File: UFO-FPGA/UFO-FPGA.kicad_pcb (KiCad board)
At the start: 2 copper layers, 68.6 x 53.3 mm, 84 parts, among them J1 Power, J2 Digital, J3 Digital/PWM, J4 Digital, J5 USB_B_Micro, Q1 2N7002, SW2 SW_DIP_x01, U1 ICE40HX8K-BG121, U10 TL071, U11 TL071, U2 FT2232HL, U3 ASDMB-12MHz, U4 MC34063AD, U5 93LC56CT-I/MS, U6 PWR convert, U7 PWR convert, U8 ADC, U9 N25Q032A13ESC40F

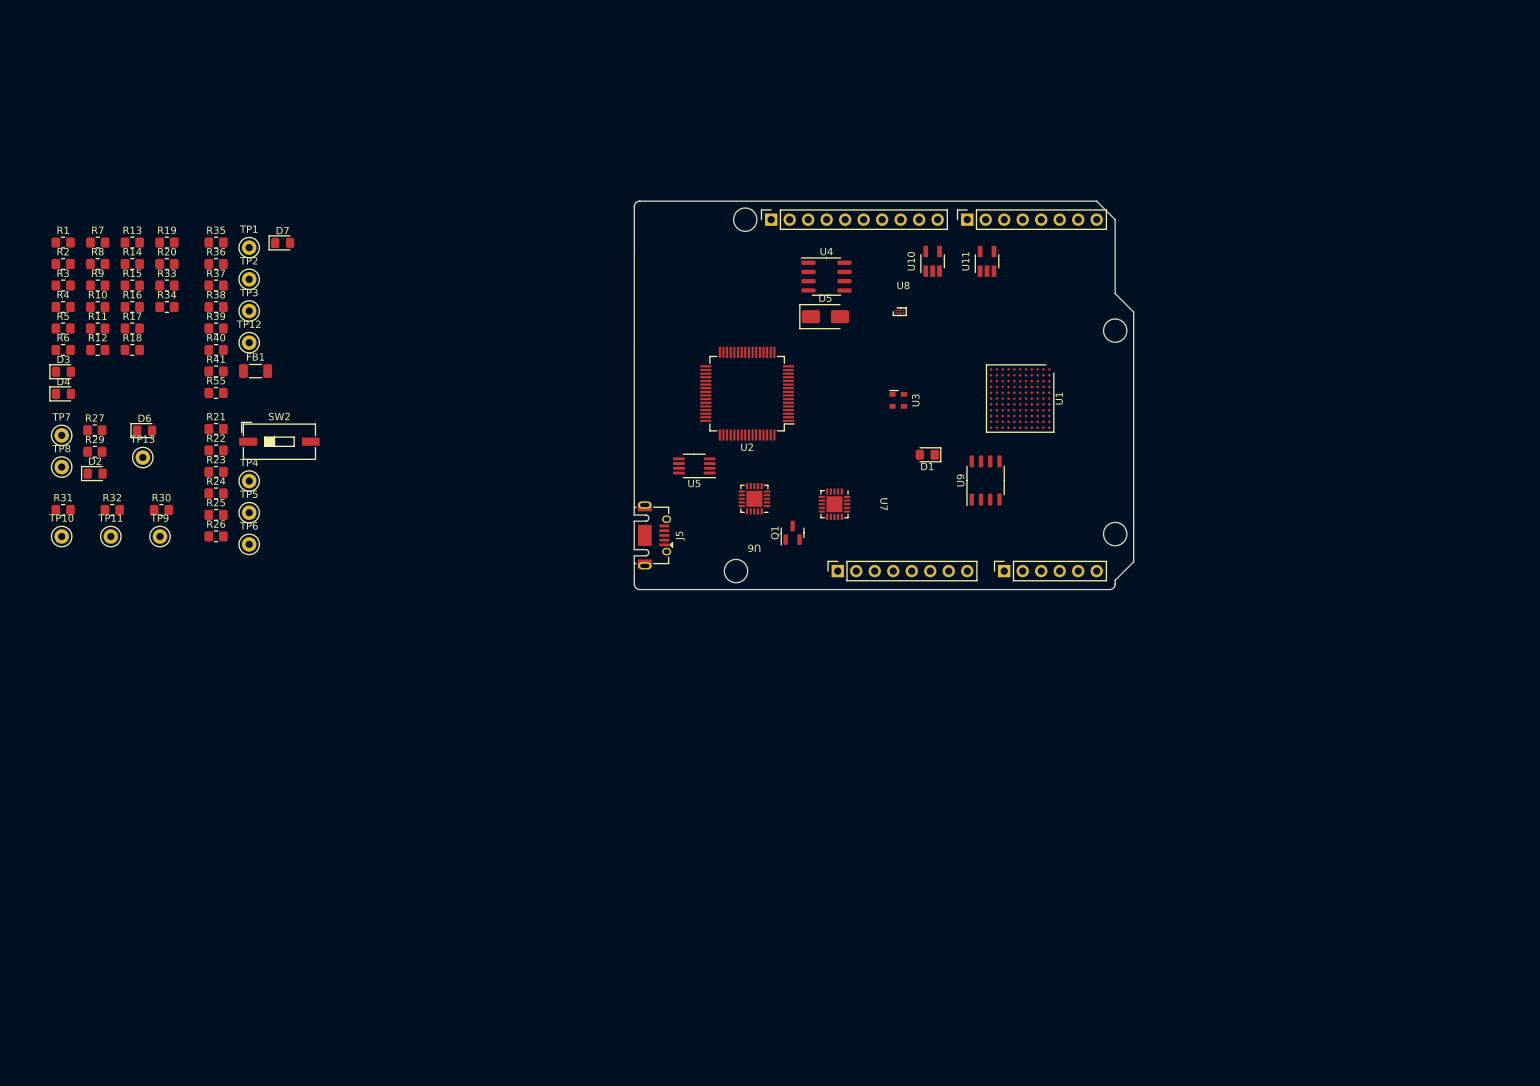
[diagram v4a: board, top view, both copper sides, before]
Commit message: PCB planes
Added:
added Power plane +1v2, +3v3 and +5v on layer 4
Ground plane on layer 2 and 5
Added signal layer 1,3 and 6
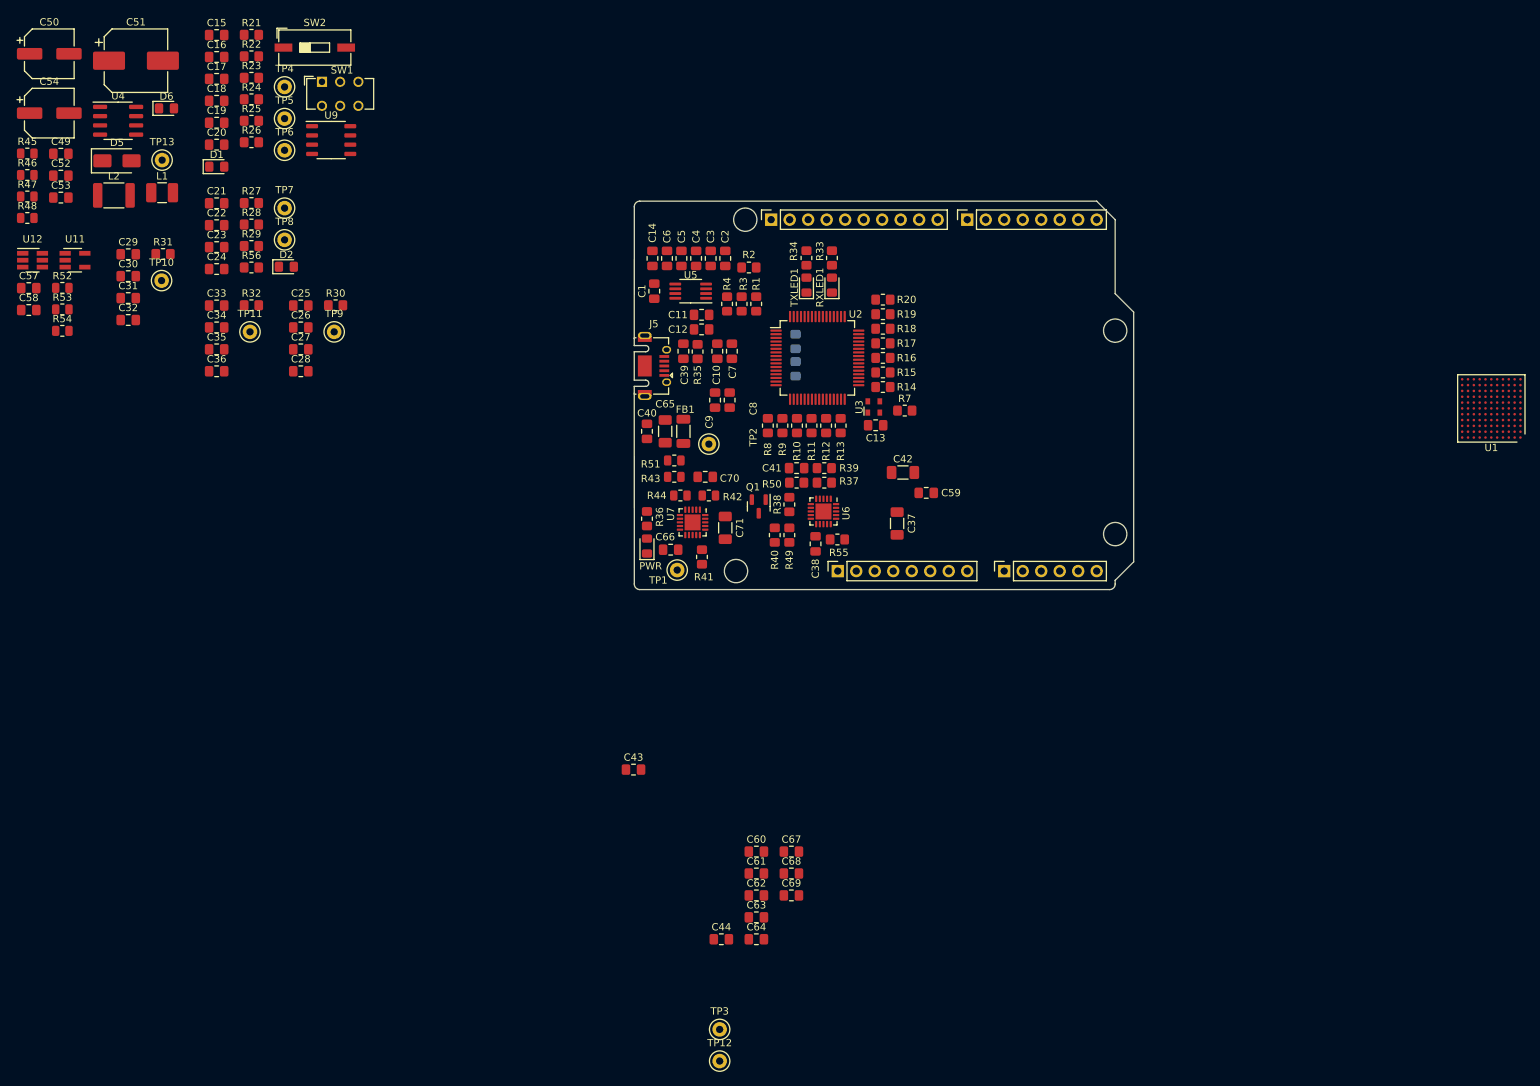
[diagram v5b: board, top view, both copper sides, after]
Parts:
- removed D3: RXLED, LED_SMD:LED_0805_2012Metric_Pad1.15x1.40mm_HandSolder
- removed D4: TXLED, LED_SMD:LED_0805_2012Metric_Pad1.15x1.40mm_HandSolder
- removed D7: POWER, LED_SMD:LED_0805_2012Metric_Pad1.15x1.40mm_HandSolder
- removed U10: TL071, Package_TO_SOT_SMD:SOT-23-5_HandSoldering
- removed U8: ADC, UFO-Footpints:WLP-8
- added C1: 100nF, Capacitor_SMD:C_0805_2012Metric_Pad1.18x1.45mm_HandSolder, F.Cu at (114.2, 60.5)
- added C10: 4u7F, Capacitor_SMD:C_0805_2012Metric_Pad1.18x1.45mm_HandSolder, F.Cu at (122.9, 68.8)
- added C11: 10uF, Capacitor_SMD:C_0805_2012Metric_Pad1.18x1.45mm_HandSolder, F.Cu at (120.8, 63.8)
- added C12: 100nF, Capacitor_SMD:C_0805_2012Metric_Pad1.18x1.45mm_HandSolder, F.Cu at (120.8, 65.8)
- added C13: 100nF, Capacitor_SMD:C_0805_2012Metric_Pad1.18x1.45mm_HandSolder, F.Cu at (144.7, 78.9)
- added C14: 100nF, Capacitor_SMD:C_0805_2012Metric_Pad1.18x1.45mm_HandSolder, F.Cu at (114.0, 56.0)
- added C15: 100nF, Capacitor_SMD:C_0805_2012Metric_Pad1.18x1.45mm_HandSolder, F.Cu at (54.2, 25.3)
- added C16: 100nF, Capacitor_SMD:C_0805_2012Metric_Pad1.18x1.45mm_HandSolder, F.Cu at (54.2, 28.3)
- added C17: 100nF, Capacitor_SMD:C_0805_2012Metric_Pad1.18x1.45mm_HandSolder, F.Cu at (54.2, 31.4)
- added C18: 10uF, Capacitor_SMD:C_0805_2012Metric_Pad1.18x1.45mm_HandSolder, F.Cu at (54.2, 34.4)
- added C19: 10uF, Capacitor_SMD:C_0805_2012Metric_Pad1.18x1.45mm_HandSolder, F.Cu at (54.2, 37.4)
- added C2: 100nF, Capacitor_SMD:C_0805_2012Metric_Pad1.18x1.45mm_HandSolder, F.Cu at (124.0, 56.0)
- added C20: 100nF, Capacitor_SMD:C_0805_2012Metric_Pad1.18x1.45mm_HandSolder, F.Cu at (54.2, 40.4)
- added C21: 100nF, Capacitor_SMD:C_0805_2012Metric_Pad1.18x1.45mm_HandSolder, F.Cu at (54.2, 48.4)
- added C22: 100nF, Capacitor_SMD:C_0805_2012Metric_Pad1.18x1.45mm_HandSolder, F.Cu at (54.2, 51.4)
- added C23: 100nF, Capacitor_SMD:C_0805_2012Metric_Pad1.18x1.45mm_HandSolder, F.Cu at (54.2, 54.5)
- added C24: 100nF, Capacitor_SMD:C_0805_2012Metric_Pad1.18x1.45mm_HandSolder, F.Cu at (54.2, 57.5)
- added C25: 100nF, Capacitor_SMD:C_0805_2012Metric_Pad1.18x1.45mm_HandSolder, F.Cu at (65.7, 62.5)
- added C26: 100nF, Capacitor_SMD:C_0805_2012Metric_Pad1.18x1.45mm_HandSolder, F.Cu at (65.7, 65.5)
- added C27: 100nF, Capacitor_SMD:C_0805_2012Metric_Pad1.18x1.45mm_HandSolder, F.Cu at (65.7, 68.5)
- added C28: 100nF, Capacitor_SMD:C_0805_2012Metric_Pad1.18x1.45mm_HandSolder, F.Cu at (65.7, 71.5)
- added C29: 100nF, Capacitor_SMD:C_0805_2012Metric_Pad1.18x1.45mm_HandSolder, F.Cu at (42.0, 55.4)
- added C3: 100nF, Capacitor_SMD:C_0805_2012Metric_Pad1.18x1.45mm_HandSolder, F.Cu at (122.0, 56.0)
- added C30: 100nF, Capacitor_SMD:C_0805_2012Metric_Pad1.18x1.45mm_HandSolder, F.Cu at (42.0, 58.4)
- added C31: 100nF, Capacitor_SMD:C_0805_2012Metric_Pad1.18x1.45mm_HandSolder, F.Cu at (42.0, 61.5)
- added C32: 100nF, Capacitor_SMD:C_0805_2012Metric_Pad1.18x1.45mm_HandSolder, F.Cu at (42.0, 64.5)
- added C33: 100nF, Capacitor_SMD:C_0805_2012Metric_Pad1.18x1.45mm_HandSolder, F.Cu at (54.2, 62.5)
- added C34: 100nF, Capacitor_SMD:C_0805_2012Metric_Pad1.18x1.45mm_HandSolder, F.Cu at (54.2, 65.5)
- added C35: 100nF, Capacitor_SMD:C_0805_2012Metric_Pad1.18x1.45mm_HandSolder, F.Cu at (54.2, 68.5)
- added C36: 100nF, Capacitor_SMD:C_0805_2012Metric_Pad1.18x1.45mm_HandSolder, F.Cu at (54.2, 71.5)
- added C37: 47uF, Capacitor_SMD:C_1206_3216Metric_Pad1.33x1.80mm_HandSolder, F.Cu at (147.6, 92.4)
- added C38: 10nF, Capacitor_SMD:C_0805_2012Metric_Pad1.18x1.45mm_HandSolder, F.Cu at (136.4, 95.2)
- added C39: 100nF, Capacitor_SMD:C_0805_2012Metric_Pad1.18x1.45mm_HandSolder, F.Cu at (118.2, 68.8)
- added C4: 100nF, Capacitor_SMD:C_0805_2012Metric_Pad1.18x1.45mm_HandSolder, F.Cu at (120.0, 56.0)
- added C40: 100nF, Capacitor_SMD:C_0805_2012Metric_Pad1.18x1.45mm_HandSolder, F.Cu at (113.2, 79.8)
- added C41: 10nF, Capacitor_SMD:C_0805_2012Metric_Pad1.18x1.45mm_HandSolder, F.Cu at (133.8, 84.8)
- added C42: 47uF, Capacitor_SMD:C_1206_3216Metric_Pad1.33x1.80mm_HandSolder, F.Cu at (148.4, 85.4)
- added C43: 10uF, Capacitor_SMD:C_0805_2012Metric_Pad1.18x1.45mm_HandSolder, F.Cu at (111.4, 126.2)
- added C44: 10uF, Capacitor_SMD:C_0805_2012Metric_Pad1.18x1.45mm_HandSolder, F.Cu at (123.5, 149.5)
- added C49: 220pF, Capacitor_SMD:C_0805_2012Metric_Pad1.18x1.45mm_HandSolder, F.Cu at (32.8, 41.6)
- added C5: 100nF, Capacitor_SMD:C_0805_2012Metric_Pad1.18x1.45mm_HandSolder, F.Cu at (118.0, 56.0)
- added C50: 100uF, Capacitor_SMD:CP_Elec_6.3x7.7, F.Cu at (31.2, 27.9)
- added C51: 470uF, Capacitor_SMD:CP_Elec_8x10.5, F.Cu at (43.1, 28.9)
- added C52: 100nF, Capacitor_SMD:C_0805_2012Metric_Pad1.18x1.45mm_HandSolder, F.Cu at (32.8, 44.6)
- added C53: 100nF, Capacitor_SMD:C_0805_2012Metric_Pad1.18x1.45mm_HandSolder, F.Cu at (32.8, 47.6)
- added C54: 100uF, Capacitor_SMD:CP_Elec_6.3x7.7, F.Cu at (31.2, 36.0)
- added C57: 100pF, Capacitor_SMD:C_0805_2012Metric_Pad1.18x1.45mm_HandSolder, F.Cu at (28.4, 60.1)
- added C58: 100pF, Capacitor_SMD:C_0805_2012Metric_Pad1.18x1.45mm_HandSolder, F.Cu at (28.4, 63.1)
- added C59: 1uF, Capacitor_SMD:C_0805_2012Metric_Pad1.18x1.45mm_HandSolder, F.Cu at (151.6, 88.2)
- added C6: 100nF, Capacitor_SMD:C_0805_2012Metric_Pad1.18x1.45mm_HandSolder, F.Cu at (116.0, 56.0)
- added C60: 1uF, Capacitor_SMD:C_0805_2012Metric_Pad1.18x1.45mm_HandSolder, F.Cu at (128.3, 137.5)
- added C61: 100nF, Capacitor_SMD:C_0805_2012Metric_Pad1.18x1.45mm_HandSolder, F.Cu at (128.3, 140.5)
- added C62: 100nF, Capacitor_SMD:C_0805_2012Metric_Pad1.18x1.45mm_HandSolder, F.Cu at (128.3, 143.5)
- added C63: 100nF, Capacitor_SMD:C_0805_2012Metric_Pad1.18x1.45mm_HandSolder, F.Cu at (128.3, 146.5)
- added C64: 10nF, Capacitor_SMD:C_0805_2012Metric_Pad1.18x1.45mm_HandSolder, F.Cu at (128.3, 149.5)
- added C65: 47uF, Capacitor_SMD:C_1206_3216Metric_Pad1.33x1.80mm_HandSolder, F.Cu at (115.8, 79.8)
- added C66: 10nF, Capacitor_SMD:C_0805_2012Metric_Pad1.18x1.45mm_HandSolder, F.Cu at (116.5, 96.0)
- added C67: 100nF, Capacitor_SMD:C_0805_2012Metric_Pad1.18x1.45mm_HandSolder, F.Cu at (133.1, 137.5)
- added C68: 100nF, Capacitor_SMD:C_0805_2012Metric_Pad1.18x1.45mm_HandSolder, F.Cu at (133.1, 140.5)
- added C69: 10nF, Capacitor_SMD:C_0805_2012Metric_Pad1.18x1.45mm_HandSolder, F.Cu at (133.1, 143.5)
- added C7: 100nF, Capacitor_SMD:C_0805_2012Metric_Pad1.18x1.45mm_HandSolder, F.Cu at (124.9, 68.8)
- added C70: 10nF, Capacitor_SMD:C_0805_2012Metric_Pad1.18x1.45mm_HandSolder, F.Cu at (121.2, 86.0)
- added C71: 47uF, Capacitor_SMD:C_1206_3216Metric_Pad1.33x1.80mm_HandSolder, F.Cu at (124.0, 93.0)
- added C8: 100nF, Capacitor_SMD:C_0805_2012Metric_Pad1.18x1.45mm_HandSolder, F.Cu at (124.6, 75.5)
- added C9: 4u7F, Capacitor_SMD:C_0805_2012Metric_Pad1.18x1.45mm_HandSolder, F.Cu at (122.6, 75.5)
- added L1: 1uH, Inductor_SMD:L_1210_3225Metric_Pad1.42x2.65mm_HandSolder, F.Cu at (46.7, 47.0)
- added L2: 180uH, Inductor_SMD:L_1812_4532Metric_Pad1.30x3.40mm_HandSolder, F.Cu at (40.0, 47.4)
- added PWR: POWER, LED_SMD:LED_0805_2012Metric_Pad1.15x1.40mm_HandSolder, F.Cu at (113.2, 95.5)
- added R28: 510R, Resistor_SMD:R_0805_2012Metric_Pad1.20x1.40mm_HandSolder, F.Cu at (58.9, 51.4)
- added R42: 12k, Resistor_SMD:R_0805_2012Metric, F.Cu at (121.8, 88.6)
- added R43: 3k, Resistor_SMD:R_0805_2012Metric, F.Cu at (117.0, 86.0)
- added R44: 100k, Resistor_SMD:R_0805_2012Metric, F.Cu at (117.8, 88.6)
- added R45: 3, Resistor_SMD:R_0805_2012Metric, F.Cu at (28.2, 41.6)
- added R46: 91k, Resistor_SMD:R_0805_2012Metric, F.Cu at (28.2, 44.5)
- added R47: 30k, Resistor_SMD:R_0805_2012Metric, F.Cu at (28.2, 47.5)
- added R48: 1.6k, Resistor_SMD:R_0805_2012Metric, F.Cu at (28.2, 50.5)
- added R49: 900, Resistor_SMD:R_0805_2012Metric_Pad1.20x1.40mm_HandSolder, F.Cu at (132.8, 94.0)
- added R50: 400, Resistor_SMD:R_0805_2012Metric_Pad1.20x1.40mm_HandSolder, F.Cu at (133.8, 86.8)
- added R51: 750R, Resistor_SMD:R_0805_2012Metric, F.Cu at (117.0, 83.8)
- added R52: 510, Resistor_SMD:R_0805_2012Metric, F.Cu at (33.0, 60.0)
- added R53: 510, Resistor_SMD:R_0805_2012Metric, F.Cu at (33.0, 63.0)
- added R54: 10, Resistor_SMD:R_0805_2012Metric, F.Cu at (33.0, 66.0)
- added R56: 130R, Resistor_SMD:R_0805_2012Metric_Pad1.20x1.40mm_HandSolder, F.Cu at (58.9, 57.2)
- added RXLED1: RXLED, LED_SMD:LED_0805_2012Metric_Pad1.15x1.40mm_HandSolder, F.Cu at (138.7, 59.7)
- added SW1: SW_Push_DPDT, Button_Switch_THT:SW_CuK_JS202011CQN_DPDT_Straight, F.Cu at (68.6, 31.8)
- added TXLED1: TXLED, LED_SMD:LED_0805_2012Metric_Pad1.15x1.40mm_HandSolder, F.Cu at (135.2, 59.7)
- added U12: MAX11116AUT+T, Package_TO_SOT_SMD:SOT-23-6_Handsoldering, F.Cu at (28.9, 56.2)
- R29: value 1 -> 1R
- R37: value 12K4 -> 12k
- R38: value 24K9 -> 24k
- R5, R6: moved to B.Cu
- moved U11 125.2 mm to (34.7, 56.2), turned to 0 degrees
- moved TP12 117.9 mm to (123.2, 166.2)
- moved TP3 117.9 mm to (123.2, 161.9)
- moved R7 113.2 mm to (148.7, 76.9)
- moved D1 105.3 mm to (54.2, 43.4), turned to 0 degrees
- moved R14 104.5 mm to (145.7, 73.7), turned to 180 degrees
- moved R15 103.8 mm to (145.7, 71.7), turned to 180 degrees
- moved R16 103.3 mm to (145.7, 69.7)
- moved R18 103.1 mm to (145.7, 65.7), turned to 180 degrees
- moved R17 103.1 mm to (145.7, 67.7)
- moved U9 101.3 mm to (69.9, 39.8), turned to 0 degrees
- moved R5 100.7 mm to (133.7, 71.2), turned to 90 degrees
- moved R6 100.6 mm to (133.7, 67.4), turned to 90 degrees
- moved R12 100.6 mm to (137.8, 79.0), turned to 90 degrees
- moved R13 100.5 mm to (139.8, 79.0), turned to 90 degrees
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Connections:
- net /Invert-5V-Dual-Ramp/-15 unfiltered renamed /Invert-5V-Dual-Ramp/-5 unfiltered
- J1 pad 1: unconnected-(J1-Pin_1-Pad1) -> Vin
- J1 pad 8: Vin -> GND
- J5 pad 6: unconnected-(J5-Shield-Pad6) -> GND
- R37 pad 1: Net-(U6-FB) -> Net-(R37-Pad1)
- R38 pad 1: GND -> Net-(R38-Pad1)
- U1 pad B5: CHSEL -> unconnected-(U1A-IOT_208-PadB5)
- U11 pad 2: VDC -> AIN1_O
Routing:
- added copper zone on In3.Cu, net +1V2
- added copper zone on In3.Cu, net +3V3
- added copper zone on In3.Cu, net +5V
- added copper zone on In1.Cu, net GND
- added copper zone on In4.Cu, net GND
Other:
- outline, holes or cut-outs redrawn
- copper layers 2 -> 6
- board text removed: "ICSP"

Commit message: PCB
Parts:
- moved U1 67.6 mm to (161.8, 72.8)
- moved C59 9.14 mm to (142.5, 89.0)
- moved C11 6.96 mm to (127.7, 63.8)
- moved C12 6.96 mm to (127.7, 65.8)
- moved C37 4.61 mm to (143.0, 92.8)
- moved C42 3.10 mm to (145.5, 86.5)
- moved R1 3.05 mm to (130.0, 59.8)
- moved R2 3.05 mm to (129.0, 54.8)
- moved R3 3.05 mm to (128.0, 59.8)
- moved R4 3.05 mm to (126.0, 59.8)
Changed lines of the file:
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@@
   )
   (footprint "Resistor_SMD:R_0805_2012Metric_Pad1.20x1.40mm_HandSolder" (layer "F.Cu")
-    (at 124.25 62.25 90)
+    (at 126 59.75 90)
     (descr "Resistor SMD 0805 (2012 Metric), square (rectangular) end terminal, IPC_7351 nominal with elongated pad for handsoldering. (Body size source: IPC-SM-782 page 72, https://www.pcb-3d.com/wordpress/wp-content/uploads/ipc-sm-782a_amendment_1_and_2.pdf), generated with kicad-footprint-generator")
     (tags "resistor handsolder")
@@
   )
   (footprint "Capacitor_SMD:C_1206_3216Metric_Pad1.33x1.80mm_HandSolder" (layer "F.Cu")
-    (at 148.4 85.4)
+    (at 145.5 86.5)
     (descr "Capacitor SMD 1206 (3216 Metric), square (rectangular) end terminal, IPC_7351 nominal with elongated pad for handsoldering. (Body size source: IPC-SM-782 page 76, https://www.pcb-3d.com/wordpress/wp-content/uploads/ipc-sm-782a_amendment_1_and_2.pdf), generated with kicad-footprint-generator")
     (tags "capacitor handsolder")
@@
   )
   (footprint "Resistor_SMD:R_0805_2012Metric_Pad1.20x1.40mm_HandSolder" (layer "F.Cu")
-    (at 126.25 62.25 90)
+    (at 128 59.75 90)
     (descr "Resistor SMD 0805 (2012 Metric), square (rectangular) end terminal, IPC_7351 nominal with elongated pad for handsoldering. (Body size source: IPC-SM-782 page 72, https://www.pcb-3d.com/wordpress/wp-content/uploads/ipc-sm-782a_amendment_1_and_2.pdf), generated with kicad-footprint-generator")
     (tags "resistor handsolder")
@@
   )
   (footprint "Resistor_SMD:R_0805_2012Metric_Pad1.20x1.40mm_HandSolder" (layer "F.Cu")
-    (at 127.25 57.25)
+    (at 129 54.75)
     (descr "Resistor SMD 0805 (2012 Metric), square (rectangular) end terminal, IPC_7351 nominal with elongated pad for handsoldering. (Body size source: IPC-SM-782 page 72, https://www.pcb-3d.com/wordpress/wp-content/uploads/ipc-sm-782a_amendment_1_and_2.pdf), generated with kicad-footprint-generator")
     (tags "resistor handsolder")
@@
   )
   (footprint "Capacitor_SMD:C_0805_2012Metric_Pad1.18x1.45mm_HandSolder" (layer "F.Cu")
-    (at 120.75 63.75 180)
+    (at 127.7125 63.75 180)
     (descr "Capacitor SMD 0805 (2012 Metric), square (rectangular) end terminal, IPC_7351 nominal with elongated pad for handsoldering. (Body size source: IPC-SM-782 page 76, https://www.pcb-3d.com/wordpress/wp-content/uploads/ipc-sm-782a_amendment_1_and_2.pdf, https://docs.google.com/spreadsheets/d/1BsfQQcO9C6DZCsRaXUlFlo91Tg2WpOkGARC1WS5S8t0/edit?usp=sharing), generated with kicad-footprint-generator")
     (tags "capacitor handsolder")
@@
   )
   (footprint "Capacitor_SMD:C_1206_3216Metric_Pad1.33x1.80mm_HandSolder" (layer "F.Cu")
-    (at 147.6 92.4 90)
+    (at 143 92.75 90)
     (descr "Capacitor SMD 1206 (3216 Metric), square (rectangular) end terminal, IPC_7351 nominal with elongated pad for handsoldering. (Body size source: IPC-SM-782 page 76, https://www.pcb-3d.com/wordpress/wp-content/uploads/ipc-sm-782a_amendment_1_and_2.pdf), generated with kicad-footprint-generator")
     (tags "capacitor handsolder")
@@
   )
   (footprint "Package_BGA:BGA-121_9.0x9.0mm_Layout11x11_P0.8mm_Ball0.4mm_Pad0.35mm_NSMD" (layer "F.Cu")
-    (at 229.2 76.6 180)
+    (at 161.75 72.75 180)
     (descr "121-ball, 0.8mm BGA (based on http://www.latticesemi.com/view_document?document_id=213)")
     (tags "BGA 0.8mm 9mm 121")
@@
   )
   (footprint "Capacitor_SMD:C_0805_2012Metric_Pad1.18x1.45mm_HandSolder" (layer "F.Cu")
-    (at 120.75 65.75 180)
+    (at 127.7125 65.75 180)
     (descr "Capacitor SMD 0805 (2012 Metric), square (rectangular) end terminal, IPC_7351 nominal with elongated pad for handsoldering. (Body size source: IPC-SM-782 page 76, https://www.pcb-3d.com/wordpress/wp-content/uploads/ipc-sm-782a_amendment_1_and_2.pdf, https://docs.google.com/spreadsheets/d/1BsfQQcO9C6DZCsRaXUlFlo91Tg2WpOkGARC1WS5S8t0/edit?usp=sharing), generated with kicad-footprint-generator")
     (tags "capacitor handsolder")
@@
   )
   (footprint "Resistor_SMD:R_0805_2012Metric_Pad1.20x1.40mm_HandSolder" (layer "F.Cu")
-    (at 128.25 62.25 -90)
+    (at 130 59.75 -90)
     (descr "Resistor SMD 0805 (2012 Metric), square (rectangular) end terminal, IPC_7351 nominal with elongated pad for handsoldering. (Body size source: IPC-SM-782 page 72, https://www.pcb-3d.com/wordpress/wp-content/uploads/ipc-sm-782a_amendment_1_and_2.pdf), generated with kicad-footprint-generator")
     (tags "resistor handsolder")
@@
   )
   (footprint "Capacitor_SMD:C_0805_2012Metric_Pad1.18x1.45mm_HandSolder" (layer "F.Cu")
-    (at 151.6 88.2)
+    (at 142.5 89)
     (descr "Capacitor SMD 0805 (2012 Metric), square (rectangular) end terminal, IPC_7351 nominal with elongated pad for handsoldering. (Body size source: IPC-SM-782 page 76, https://www.pcb-3d.com/wordpress/wp-content/uploads/ipc-sm-782a_amendment_1_and_2.pdf, https://docs.google.com/spreadsheets/d/1BsfQQcO9C6DZCsRaXUlFlo91Tg2WpOkGARC1WS5S8t0/edit?usp=sharing), generated with kicad-footprint-generator")
     (tags "capacitor handsolder")
@@
     (polygon
       (pts
-        (xy 120.6 91.4)
-        (xy 117 88.6)
-        (xy 117 84.8)
-        (xy 119.8 84.8)
-        (xy 119.8 78.8)
-        (xy 120 68.8)
+        (xy 119.6 91.5)
+        (xy 116.75 89.25)
+        (xy 116.75 85)
+        (xy 120.5 85)
+        (xy 120.5 78.8)
+        (xy 120.5 68.75)
         (xy 118 65.2)
         (xy 112.4 65)
@@
         (xy 129.2 87.8)
         (xy 127.6 91)
-        (xy 127.2 91.4)
+        (xy 127.2 91.5)
       )
     )

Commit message: ubs shield
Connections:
- J5 pad 6: GND -> unconnected-(J5-Shield-Pad6)
- U2 pad 49: unconnected-(U2-VREGOUT-Pad49) -> +1V8
